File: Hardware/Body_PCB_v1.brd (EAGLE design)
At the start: 112 x 111.6 mm, 66 parts, among them P1:C1 10uF, P1:JP1 THROTTLE, P1:JP3 OBD, P1:JP4 DOC, P1:R1 22k, P1:R3 22k, P1:R4 39R, P1:U$1 SJ-43514_HEADPHONES_3.5MM_X4

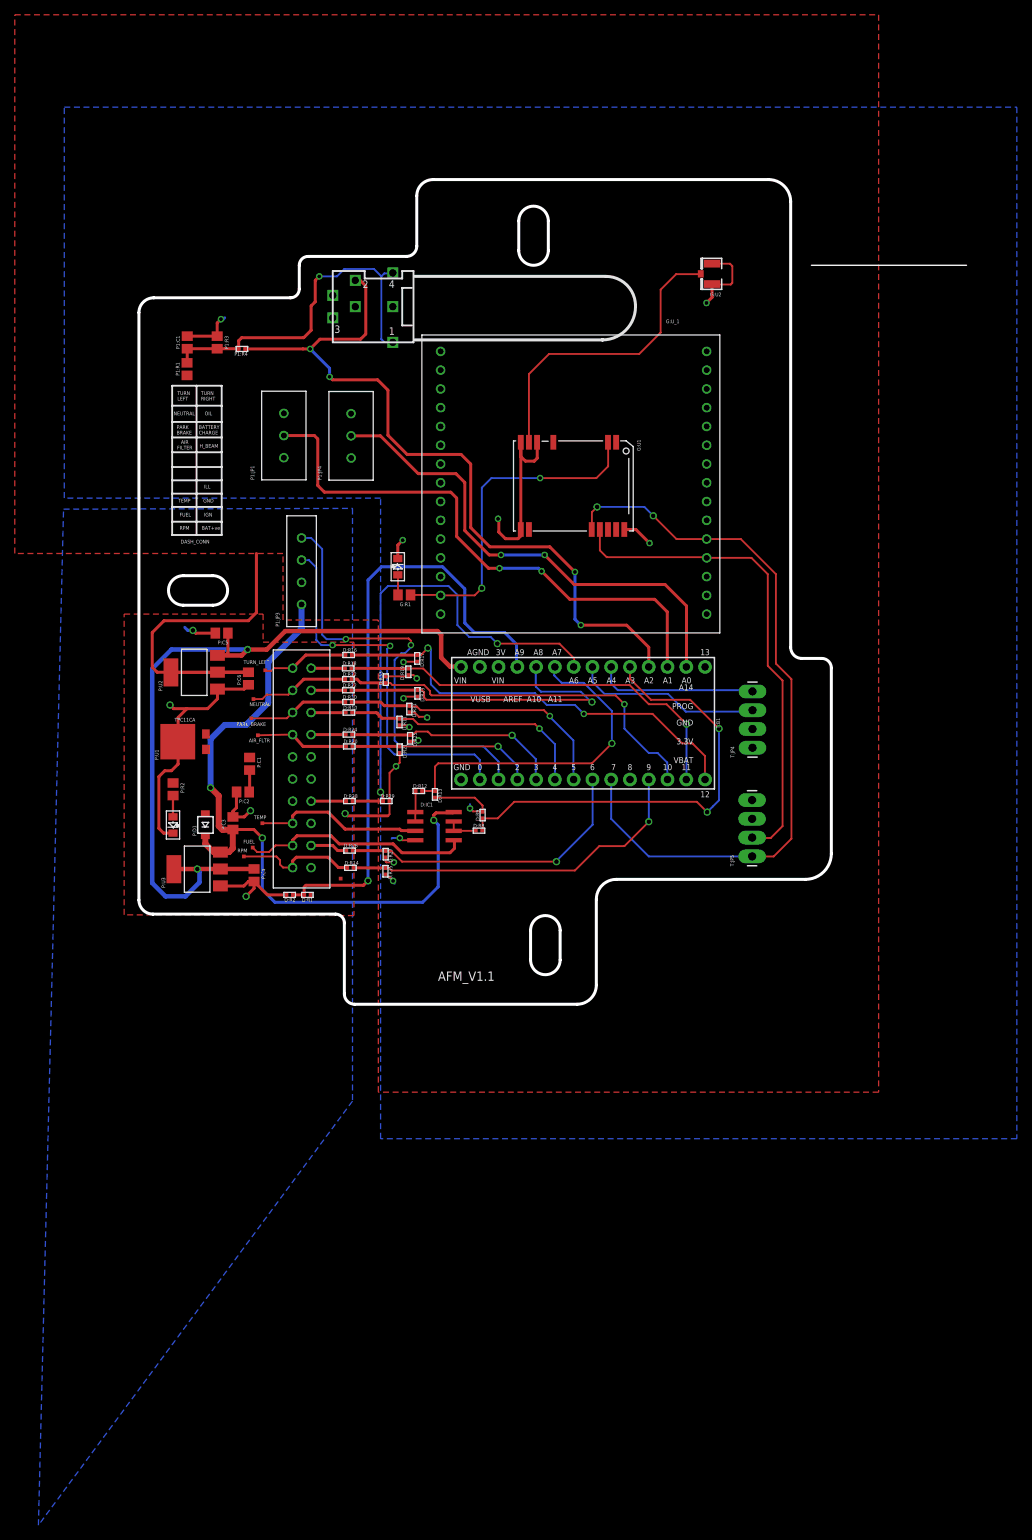
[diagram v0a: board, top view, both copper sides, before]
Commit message: Addition of 2D Vertical Surface Code
- Added code for Vertical Steps
- No feedback from Z Axis motors
- Andrew. This is for you.
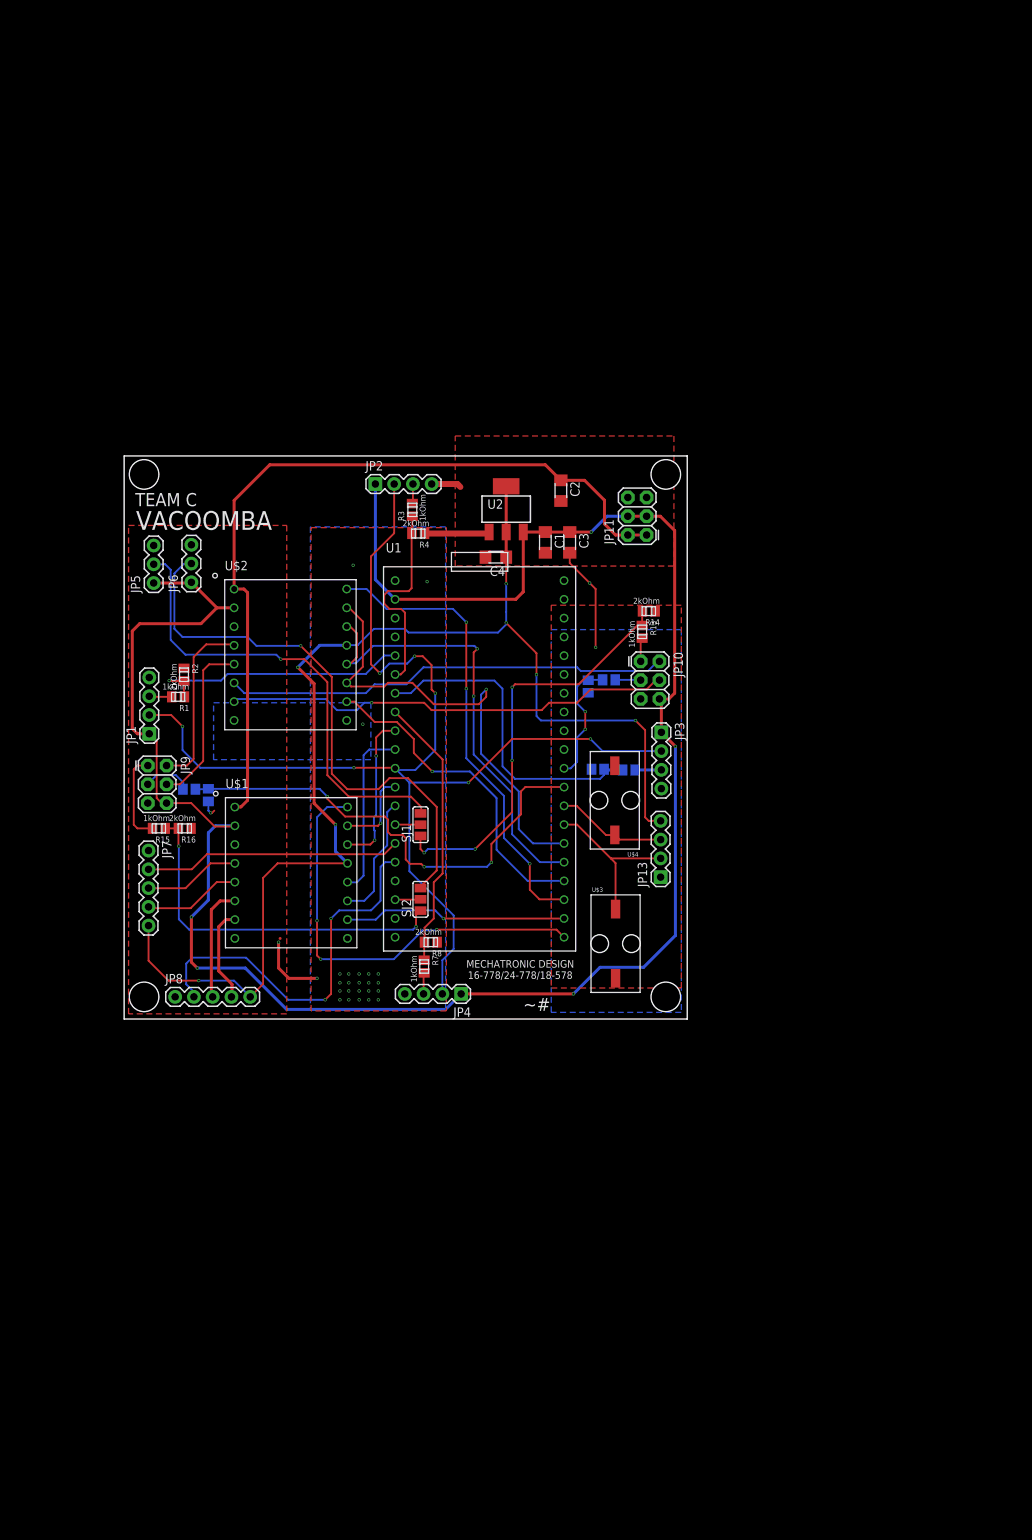
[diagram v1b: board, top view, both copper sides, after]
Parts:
- removed D:IC1: LM358D, linear:SO08
- removed D:R1, D:R10, D:R11, D:R12, D:R13, D:R14, D:R15, D:R16, D:R17, D:R18, D:R19, D:R2, D:R20, D:R21, D:R22, D:R23, D:R24, D:R25, D:R26, D:R27, D:R28, D:R29, D:R30, D:R31, D:R32, D:R33, D:R8, D:R9, P1:R4: 39R, Carnot:R0402
- removed D:TP1, D:TP2, D:TP3, D:TP4, D:TP5, D:TP6, D:TP7, D:TP8: (no value), SparkFun-Passives:PAD.02X.02
- removed D:U$1: DASH_CONNECTOR'PITCH_3MM', Carnot:20PINCONN
- removed G:1PPS, P:1PPS1: LED_0805, Carnot:LED0805
- removed G:R1, P:R2: 1k, Carnot:R0805
- removed G:U1: NEO-6M, Carnot:28P-1.1-16.0X12.2
- removed G:U2: U.FL, Carnot:U.FL
- removed G:U_1: SKYTRAQ_HORIZONTAL_SHIELD, Carnot:SKYTRAQ_HORIZONTAL
- removed P1:C1, P:C3, P:C4, P:C5, P:C6: 10uF, Carnot:C0805
- removed P1:JP1: THROTTLE, Carnot:3P_3MM
- removed P1:JP3: OBD, Carnot:4P_3MM
- removed P1:JP4: DOC, Carnot:3P_3MM
- removed P1:R1, P1:R3: 22k, Carnot:R0805
- removed P1:U$1: SJ-43514_HEADPHONES_3.5MM_X4, my_parts:SJ-43514_HEADPHONES-3.5MM_X4
- removed P:C1: 0.1uF/100V, Carnot:C0805
- removed P:C2: 1uF/100V, Carnot:C0805
- removed P:D1: DB2W60400L, Carnot:DB2W60400L
- removed P:U1: TPC11CA, Carnot:TPC11CA
- removed P:U2, P:U3: 1117, Carnot:SOT223
- removed T:B1: TEENSY-3.1SILK, SparkFun-Boards:TEENSY-3.1
- removed T:JP4, T:JP5: (no value), SparkFun-Connectors:1X04_LONGPADS
- added C1, C2, C3, C4: (no value), Team_Ojas_OVPowar:1206
- added JP1, JP13, JP2, JP3, JP4: (no value), SparkFun-Connectors:1X04
- added JP10, JP11, JP9: FEMALE 2x3, SparkFun-Connectors:2X3
- added JP5, JP6: (no value), SparkFun-Connectors:1X03
- added JP7, JP8: (no value), SparkFun-Connectors:1X05
- added R1, R11, R13, R15, R3, R5, R7, R9: 1kOhm, Team_Ojas_OVPowar:0805
- added R10, R12, R14, R16, R2, R4, R6, R8: 2kOhm, Team_Ojas_OVPowar:0805
- added SJ1, SJ2: (no value), jumper:SJ_2
- added U$1, U$2: TB6612FNG, Team_Ojas_OVPowar:TB6612FNG_DRIVER
- added U$3, U$4: MOLEX-SMT-2-PIN-VERTICAL, Team_Ojas_OVPowar:430450215
- added U1: MBED_NXP_LPC1768, Team_Ojas_OVPowar:40_PDIP
- added U2: 1117, Carnot_AfterMarket_v2.2:SOT223
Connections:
- removed net 12V_REGULATED: D:IC1.8, P1:JP3.1, P:C3.1, P:D1.C, P:U3.3
- removed net 5V: P:C4.1, P:C5.1, P:U2.3, P:U3.2, P:U3.4, T:B1.VIN
- removed net AIR_FLTR: D:R20.P$2, D:R21.P$1, T:B1.2
- removed net BATTERY_CHARGE: D:R10.P$2, D:R11.P$1, T:B1.4
- removed net D:AIR_FLTR_12V: D:R20.P$1, D:TP4.P$1, D:U$1.7
- removed net D:BATTERY_CHARGE_12V: D:R10.P$1, D:U$1.18
- removed net D:FUEL_SNS_12V: D:IC1.5, D:TP2.P$1, D:U$1.2
- removed net D:HIGH_BEAM_12V: D:R24.P$1, D:U$1.17
- removed net D:IGN_12V: D:R26.P$1, D:U$1.12
- removed net D:ILLUMINATION_12V: D:R28.P$1, D:U$1.14
- removed net D:N$3: D:IC1.1, D:IC1.2, D:R12.P$1
- removed net D:N$6: D:IC1.6, D:IC1.7, D:R8.P$1
- removed net D:NEUTRAL_12V: D:R32.P$1, D:TP6.P$1, D:U$1.9
- removed net D:OIL_PRESSURE_12V: D:R22.P$1, D:U$1.19
- removed net D:PARK_BRAKE_12V: D:R30.P$1, D:TP5.P$1, D:U$1.8
- removed net D:RPM_IN_12V: D:R14.P$1, D:TP1.P$1, D:U$1.1
- removed net D:TEMP_SNS_12V: D:IC1.3, D:TP3.P$1, D:U$1.3
- removed net D:TURN_LEFT_12V: D:R16.P$1, D:TP7.P$1, D:U$1.10
- removed net D:TURN_RIGHT_12V: D:R18.P$1, D:U$1.20
- removed net DOC: P1:JP4.2, T:B1.14
- removed net FUEL_SNS: D:R8.P$2, D:R9.P$1, T:B1.17
- removed net G:GPS_UART_RX2: G:U_1.7
- removed net G:GPS_UART_TX2: G:U_1.6
- removed net G:N$10: G:1PPS.P$2, G:R1.2
- removed net G:N$8: G:U1.22
- removed net G:PPS: G:R1.1, G:U1.3, G:U_1.29
- removed net G:RF_IN: G:U1.11, G:U2.3
- removed net GPS_UART_RX1: G:U1.21, G:U_1.4, T:JP5.2
- removed net GPS_UART_TX1: G:U1.20, G:U_1.5, T:B1.7, T:JP5.1
- removed net HIGH_BEAM: D:R24.P$2, D:R25.P$1, T:B1.3
- removed net IGN: D:R26.P$2, D:R27.P$1, T:B1.6
- removed net ILLUMINATION: D:R28.P$2, D:R29.P$1, T:B1.20
- removed net N$1: D:R1.P$2, D:R2.P$1, T:B1.23
- removed net NEUTRAL: D:R32.P$2, D:R33.P$1, T:B1.10
- removed net OIL_PRESSURE: D:R22.P$2, D:R23.P$1, T:B1.22
- removed net P1:VIRTUAL_GND: P1:C1.1, P1:R1.2, P1:R3.2, P1:R4.P$2, P1:U$1.1, P1:U$1.4
- removed net P:N$2: P:1PPS1.P$2, P:R2.2
- removed net P:N$7: P:C1.2, P:C2.1
- removed net PARK_BRAKE: D:R30.P$2, D:R31.P$1, T:B1.5
- removed net RPM_IN: D:R14.P$2, D:R15.P$1, T:B1.9
- removed net RPM_I_IN: P1:R4.P$1, P1:U$1.2, T:B1.16
- removed net T:3V: T:B1.3V
- removed net T:SCL: T:B1.19, T:JP4.3
- removed net T:SDA: T:B1.18, T:JP4.4
- removed net TEMP_SNS: D:R12.P$2, D:R13.P$1, T:B1.21
- removed net THROTTLE: P1:JP1.2, T:B1.15
- removed net TURN_LEFT: D:R16.P$2, D:R17.P$1, T:B1.12
- removed net TURN_RIGHT: D:R18.P$2, D:R19.P$1, T:B1.11
- removed net UART_RX: P1:JP3.3, T:B1.0
- removed net UART_TX: P1:JP3.4, T:B1.1
- removed net VBAT_12V: D:R1.P$1, D:TP8.P$1, D:U$1.11, P:C1.1, P:D1.A, P:R2.1, P:U1.P1, P:U1.P2
- new net 12VIN: C2.1, JP11.1, JP11.2, U$1.1, U$2.1
- new net 5VIN: C1.1, C3.1, JP1.1, JP10.6, JP11.3, JP11.4, JP2.1, JP3.1, JP4.1, JP5.1, JP6.1, JP9.6, U$1.2, U$2.2, U1.2, U2.3
- new net EXTRA1: SJ1.2, U1.14
- new net EXTRA2: SJ2.2, U1.18
- new net EXTRA_ANALOG1: U1.19
- new net EXTRA_ANALOG2: U1.20
- new net PRESSURE_SENSOR: U1.17
- new net SERVO1: JP5.2, SJ1.3
- new net SERVO2: JP6.2, SJ2.3
- new net SOLENOID1: JP13.2, U$3.P$1, U1.27
- new net SOLENOID2: JP13.3, U$4.P$1, U1.28
- new net ULTRASONIC_BOTTOM_ECHO: R7.P$1, R8.P$2, U1.8
- new net ULTRASONIC_BOTTOM_ECHO_5V: JP4.3, R7.P$2
- new net ULTRASONIC_LEFT_ECHO: R1.P$1, R2.P$2, U1.5
- new net ULTRASONIC_LEFT_ECHO_5V: JP1.3, R1.P$2
- new net ULTRASONIC_RIGHT_ECHO: R5.P$1, R6.P$2, U1.7
- new net ULTRASONIC_RIGHT_ECHO_5V: JP3.3, R5.P$2
- new net ULTRASONIC_TOP_ECHO: R3.P$1, R4.P$2, U1.6
- new net ULTRASONIC_TOP_ECHO_5V: JP2.3, R3.P$2
- new net ULTRASONIC_TRIGGER: JP1.2, JP2.2, JP3.2, JP4.2, U1.11
- new net X+: JP7.3, U$1.4
- new net X-: JP7.4, U$1.5
- new net X_AXIS_DOWN: U$1.15, U1.12
- new net X_AXIS_SPEED: U$1.16, U1.21
- new net X_AXIS_UP: U$1.14, U1.9
- new net X_POS: JP7.2, U1.15
- new net Y+: JP8.3, U$1.6
- new net Y-: JP8.4, U$1.7
- new net Y_AXIS_DOWN: U$1.11, U1.13
- new net Y_AXIS_SPEED: U$1.10, U1.22
- new net Y_AXIS_UP: U$1.12, U1.10
- new net Y_POS: JP8.2, U1.16
- new net Z1+: JP9.2, U$2.4
- new net Z1-: JP9.4, U$2.5
- new net Z1_POS+: R10.P$2, R9.P$1, U1.30
- new net Z1_POS+_5V: JP10.3, R9.P$2
- new net Z1_POS-: R13.P$1, R14.P$2, SJ1.1
- new net Z1_POS-_5V: JP10.1, R13.P$2
- new net Z2+: JP10.2, U$2.6
- new net Z2-: JP10.4, U$2.7
- new net Z2_POS+: R11.P$1, R12.P$2, U1.29
- new net Z2_POS+_5V: JP9.3, R11.P$2
- new net Z2_POS-: R15.P$1, R16.P$2, SJ2.1
- new net Z2_POS-_5V: JP9.1, R15.P$2
- new net Z_AXIS1_SPEED: U$2.16, U1.23
- new net Z_AXIS2_SPEED: U$2.10, U1.24
- new net Z_AXIS_DOWN: U$2.11, U$2.15, U1.26
- new net Z_AXIS_UP: U$2.12, U$2.14, U1.25
- net 3.3V: now also C4.1, JP13.4, JP7.5, JP8.5, U$1.13, U$2.13, U2.2, U2.4; no longer G:U1.23, G:U_1.1, G:U_1.19, G:U_1.20, P1:JP1.1, P1:JP4.1, P1:R1.1, P:C6.2, P:U2.2, P:U2.4, T:JP4.1, T:JP5.3
- net GND: now also C1.2, C2.2, C3.2, C4.2, JP1.4, JP10.5, JP11.5, JP11.6, JP13.1, JP2.4, JP3.4, JP4.4, JP5.3, JP6.3, JP7.1, JP8.1, JP9.5, R10.P$1, R12.P$1, R14.P$1, R16.P$1, R2.P$1, R4.P$1, R6.P$1, R8.P$1, U$1.3, U$1.8, U$1.9, U$2.3, U$2.8, U$2.9, U$3.P$2, U$4.P$2, U1.1, U2.1; no longer D:IC1.4, D:R11.P$2, D:R13.P$2, D:R15.P$2, D:R17.P$2, D:R19.P$2, D:R2.P$2, D:R21.P$2, D:R23.P$2, D:R25.P$2, D:R27.P$2, D:R29.P$2, D:R31.P$2, D:R33.P$2, D:R9.P$2, D:U$1.13, G:1PPS.P$3, G:U1.10, G:U1.12, G:U1.13, G:U1.24, G:U2.1, G:U2.2, G:U_1.2, G:U_1.30, P1:C1.2, P1:JP1.3, P1:JP3.2, P1:JP4.3, P1:R3.1, P:1PPS1.P$3, P:C2.2, P:C3.2, P:C4.2, P:C5.2, P:C6.1, P:U1.PC, P:U2.1, P:U3.1, T:B1.AGND, T:B1.GND1, T:JP4.2, T:JP5.4
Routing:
- net 5VIN: track 0.00 -> 279.0 mm, vias 0 -> 5
- net ULTRASONIC_TRIGGER: track 0.00 -> 164.4 mm, vias 0 -> 7
- net 3.3V: track 51.7 -> 172.5 mm, vias 0 -> 7
- net GND: track 153.3 -> 38.7 mm, vias 21 -> 28
- net 12VIN: track 0.00 -> 107.8 mm
- net 5V: track 105.1 -> 0.00 mm, vias 2 -> 0
- net RPM_I_IN: track 103.7 -> 0.00 mm, vias 4 -> 0
- net GPS_UART_TX1: track 100.8 -> 0.00 mm, vias 2 -> 0
- net 12V_REGULATED: track 97.1 -> 0.00 mm, vias 3 -> 0
- net N$1: track 83.2 -> 0.00 mm, vias 1 -> 0
- net SERVO2: track 0.00 -> 76.6 mm, vias 0 -> 1
- net THROTTLE: track 76.0 -> 0.00 mm, vias 2 -> 0
- net DOC: track 67.0 -> 0.00 mm, vias 2 -> 0
- net GPS_UART_RX1: track 66.6 -> 0.00 mm
- net ILLUMINATION: track 66.6 -> 0.00 mm, vias 2 -> 0
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- added copper zone on layer 1, net GND
- removed copper zone on layer 1, net 3.3V
- removed copper zone on layer 1, net VBAT_12V
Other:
- board size 112 x 111.6 mm -> 76.2 x 76.2 mm
- board text added: "MECHATRONIC DESIGN 16-778/24-778/18-578"
- board text added: "TEAM C"
- board text added: "VACOOMBA"
- board text added: "~#"
- board text removed: "48 Document Layer is the Border for Box."
- board text removed: "AFM_V1.1"
- board text removed: "AIR FILTER"
- board text removed: "AIR_FLTR"
- board text removed: "BAT+ve"
- board text removed: "BATTERY CHARGE"
- board text removed: "DASH_CONN"
- board text removed: "FUEL"
- board text removed: "GND"
- board text removed: "H_BEAM"
- board text removed: "IGN"
- board text removed: "ILL"
- board text removed: "NEUTRAL"
- board text removed: "OIL"
- board text removed: "PARK BRAKE"
- board text removed: "PARK_BRAKE"
- board text removed: "RPM"
- board text removed: "TEMP"
- board text removed: "TURN LEFT"
- board text removed: "TURN RIGHT"
- board text removed: "TURN_LEFT"
- board text removed: "Test Points are given around the Connector."
- board text removed: "The Aux Cable Terminal will fit in the area assigned"
